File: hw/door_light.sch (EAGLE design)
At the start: 28 parts, among them IC1 TINY13-20SSU, Q1 BSP250, T2 KP-3216P3C, U1 MC33063ADE4

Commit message: fixed IR led size (was 805, should be 1206)
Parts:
- LED2: device led:LEDCHIPLED_0805 -> led:LEDCHIPLED_1206
- T1: value (none) -> n-mosfet
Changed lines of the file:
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@@
 <part name="SUPPLY24" library="supply2" deviceset="0V" device=""/>
 <part name="SUPPLY25" library="supply2" deviceset="0V" device=""/>
-<part name="LED2" library="led" deviceset="LED" device="CHIPLED_0805" value="IR"/>
+<part name="LED2" library="led" deviceset="LED" device="CHIPLED_1206" value="IR"/>
 <part name="LED1" library="led" deviceset="LED" device="CHIPLED_0603" value="RED"/>
 <part name="R6" library="rcl" deviceset="R-EU_" device="R0603" value="470R"/>
@@
 <part name="SUPPLY28" library="supply2" deviceset="0V" device=""/>
 <part name="Q1" library="transistor-fet" deviceset="BSP170P" device="" value="BSP250"/>
-<part name="T1" library="zetex" deviceset="NMOSSOT23" device=""/>
+<part name="T1" library="zetex" deviceset="NMOSSOT23" device="" value="n-mosfet"/>
 <part name="SJ1" library="jumper" deviceset="SJ" device="W" value="PWR"/>
 <part name="SJ2" library="jumper" deviceset="SJ" device="W" value="LIGHT"/>

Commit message: replaced fuse with the one of a proper type and size (1812)
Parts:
- F1: value 1206L035YR (F750mA) -> SD075-16 (F750mA)
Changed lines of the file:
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@@
 <part name="U1" library="Texas Instruments_By_element14_Batch_1" deviceset="MC33063ADE4" device=""/>
 <part name="SUPPLY26" library="supply2" deviceset="+4.1V" device="" value="Vbatt"/>
-<part name="F1" library="rcl" deviceset="R-EU_" device="MELF0207W" value="1206L035YR (F750mA)"/>
+<part name="F1" library="rcl" deviceset="R-EU_" device="MELF0207W" value="SD075-16 (F750mA)"/>
 <part name="R7" library="rcl" deviceset="R-EU_" device="R0402" value="10kR"/>
 <part name="D1" library="diode" deviceset="MBRS130LT3" device="" value=" MBRS140T3G"/>

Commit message: 180R size changed from 1206 to 603
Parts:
- R1: device rcl:R-EU_R0603 -> rcl:R-EU_M1206
- R2: device rcl:R-EU_M1206 -> rcl:R-EU_R0603
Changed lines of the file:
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@@
 <part name="C4" library="rcl" deviceset="CPOL-EU" device="153CLV-0810" value="100uF"/>
 <part name="L1" library="rcl" deviceset="L-EU" device="PIS2816" value="150uH"/>
-<part name="R2" library="rcl" deviceset="R-EU_" device="M1206" value="180R"/>
-<part name="R1" library="rcl" deviceset="R-EU_" device="R0603" value="0.22R"/>
+<part name="R2" library="rcl" deviceset="R-EU_" device="R0603" value="180R"/>
+<part name="R1" library="rcl" deviceset="R-EU_" device="M1206" value="0.22R"/>
 <part name="SUPPLY13" library="supply2" deviceset="0V" device=""/>
 <part name="SUPPLY20" library="supply2" deviceset="0V" device=""/>

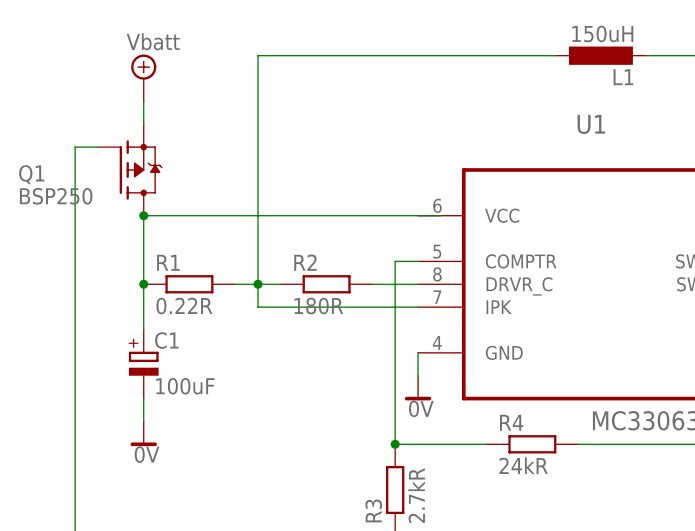
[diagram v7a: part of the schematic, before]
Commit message: DC/DC converter is nowe powered...
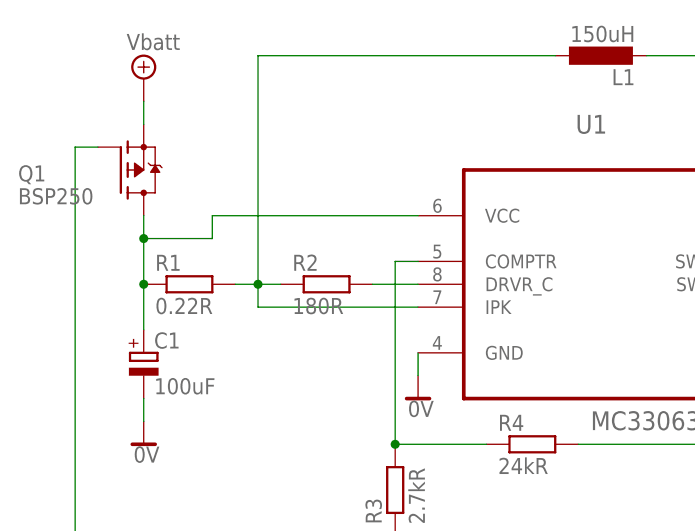
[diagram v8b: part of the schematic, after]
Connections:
- net N$3: now also U1.VCC
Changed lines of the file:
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@@
 <pinref part="C1" gate="G$1" pin="+"/>
 <wire x1="-35.56" y1="127" x2="-35.56" y2="132.08" width="0.1524" layer="91"/>
-<wire x1="-2.54" y1="139.7" x2="-35.56" y2="139.7" width="0.1524" layer="91"/>
-<wire x1="-35.56" y1="139.7" x2="-35.56" y2="132.08" width="0.1524" layer="91"/>
+<wire x1="-35.56" y1="139.7" x2="-35.56" y2="137.16" width="0.1524" layer="91"/>
 <junction x="-35.56" y="132.08"/>
 <pinref part="Q1" gate="G$1" pin="D"/>
-<junction x="-35.56" y="139.7"/>
+<pinref part="U1" gate="A" pin="VCC"/>
+<wire x1="-35.56" y1="137.16" x2="-35.56" y2="132.08" width="0.1524" layer="91"/>
+<wire x1="-5.08" y1="139.7" x2="-27.94" y2="139.7" width="0.1524" layer="91"/>
+<wire x1="-27.94" y1="139.7" x2="-27.94" y2="137.16" width="0.1524" layer="91"/>
+<wire x1="-27.94" y1="137.16" x2="-35.56" y2="137.16" width="0.1524" layer="91"/>
+<junction x="-35.56" y="137.16"/>
 </segment>
 </net>
